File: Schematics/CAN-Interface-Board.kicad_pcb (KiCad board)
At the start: 4 copper layers, 165.1 x 100 mm, 56 parts, among them CN1 Limit Switch Connector 1, CN2 Limit Switch Connector 2, CN3 Encoder Connector, CN5 XY-B3B-XH-A, CN6 MOLEX_26013114, CN7 MOLEX_CAN_IN, CN8 MOLEX_CAN_OUT, J1 USB_C_Receptacle, J2 Conn_01x04_Pin, J4 Conn_01x04_Pin, Q1 INA180A2, U1 SN65HVD230, U2 LD1117S33TR, U3 STM32F405RGTx

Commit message: inital layout started, refining stage
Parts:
- removed CBulk1: 4.7u, Capacitor_SMD:C_0805_2012Metric_Pad1.18x1.45mm_HandSolder
- removed CN5: XY-B3B-XH-A, custom footprints:CONN-TH_3P-P2.50_A2501WV2-3P
- removed CN6: MOLEX_26013114, custom footprints:MOLEX 26013114
- removed CN7: MOLEX_CAN_IN, custom footprints:MOLEX 26013114
- removed CN8: MOLEX_CAN_OUT, custom footprints:MOLEX 26013114
- removed J4: Conn_01x04_Pin, Connector_PinHeader_2.54mm:PinHeader_1x04_P2.54mm_Vertical
- added BootSwitch1: SAMZO G4R0015010, myFootprints:SAMZO G4R0015010, F.Cu at (153.2, 86.0)
- added C18: 100nf, Capacitor_SMD:C_0805_2012Metric_Pad1.18x1.45mm_HandSolder, F.Cu at (144.2, 58.8)
- added C20: 18p, Capacitor_SMD:C_0805_2012Metric_Pad1.18x1.45mm_HandSolder, F.Cu at (146.6, 55.0)
- added C21: 100nf, Capacitor_SMD:C_0805_2012Metric_Pad1.18x1.45mm_HandSolder, F.Cu at (130.1, 72.4)
- added C22: 100nf, Capacitor_SMD:C_0805_2012Metric_Pad1.18x1.45mm_HandSolder, F.Cu at (130.1, 75.4)
- added C23: 100nf, Capacitor_SMD:C_0805_2012Metric_Pad1.18x1.45mm_HandSolder, F.Cu at (130.1, 78.4)
- added C24: 100nf, Capacitor_SMD:C_0805_2012Metric_Pad1.18x1.45mm_HandSolder, F.Cu at (130.0, 64.4)
- added C25: 100nf, Capacitor_SMD:C_0805_2012Metric_Pad1.18x1.45mm_HandSolder, F.Cu at (130.0, 67.4)
- added C26: 1uf, Capacitor_SMD:C_0805_2012Metric_Pad1.18x1.45mm_HandSolder, F.Cu at (145.8, 94.0)
- added C27: 100nf, Capacitor_SMD:C_0805_2012Metric_Pad1.18x1.45mm_HandSolder, F.Cu at (145.8, 101.0)
- added C28: 1uf, Capacitor_SMD:C_0805_2012Metric_Pad1.18x1.45mm_HandSolder, F.Cu at (145.8, 103.2)
- added C29: 47uf, Capacitor_SMD:C_0805_2012Metric_Pad1.18x1.45mm_HandSolder, F.Cu at (145.8, 105.5)
- added C30: 4.7u, Capacitor_SMD:C_0805_2012Metric_Pad1.18x1.45mm_HandSolder, F.Cu at (141.2, 72.8)
- added CAN_IN1: CAN, myFootprints:MOLEX_26013114, F.Cu at (148.1, 44.2)
- added CAN_OUT1: CAN, myFootprints:MOLEX_26013114, F.Cu at (138.7, 44.2)
- added CN4: XY-B3B-XH-A, myFootprints:JST_B3B-XH-A, F.Cu at (156.2, 106.0)
- added D2: D_Schottky, Diode_SMD:D_2114_3652Metric, F.Cu at (120.5, 85.5)
- added D4: SRV05-4.TCT, myFootprints:SOT95P280X145-6N, F.Cu at (120.9, 70.8)
- added J3: Micro_SD_Card, Connector_Card:microSD_HC_Molex_104031-0811, F.Cu at (116.0, 54.5)
- added PowerIn1: 2 pin Molex, myFootprints:MOLEX_26013114, F.Cu at (142.6, 115.6)
- added R10: 10k, Resistor_SMD:R_0805_2012Metric_Pad1.20x1.40mm_HandSolder, F.Cu at (134.8, 68.5)
- added R13: 10k, Resistor_SMD:R_0805_2012Metric_Pad1.20x1.40mm_HandSolder, F.Cu at (112.5, 94.5)
- added R9: 10k, Resistor_SMD:R_0805_2012Metric_Pad1.20x1.40mm_HandSolder, F.Cu at (125.2, 52.4)
- added RSTSwitch1: SAMZO G4R0015010, myFootprints:SAMZO G4R0015010, F.Cu at (153.2, 80.5)
- added U4: MPL3115A2R1, myFootprints:PSON80P300X300X100-8N, F.Cu at (134.8, 74.0)
- added U5: LSM6DS3TR-C, myFootprints:LGA-14-2.5X3MM, F.Cu at (135.0, 65.0)
- added U6: TPS22917DBVR, myFootprints:SOT95P280X145-6N, F.Cu at (145.8, 97.2)
- added Y1: 8mhz, Crystal:Crystal_SMD_3225-4Pin_3.2x2.5mm_HandSoldering, F.Cu at (150.5, 54.8)
- C1, C2: value 100nF -> 100nf
- C10: value 2.2u -> 100nf
- C13, C17: value 100nf -> 1u
- C16, C7: value 1u -> 100nf
- C19: value 100nf -> 18p; footprint Resistor_SMD:R_0805_2012Metric_Pad1.20x1.40mm_HandSolder -> Capacitor_SMD:C_0805_2012Metric_Pad1.18x1.45mm_HandSolder
- C3: value 10uF -> 100nf
- C4: value 100nF -> 1u
- C5: value 100nF -> 4.7u
- C8: value 100nf -> 2.2u
- CN1, CN2: footprint custom footprints:JST B2B-XH-A(LF)(SN) -> myFootprints:JST_B2B-XH-A_LF__SN_
- CN3: value Encoder Connector -> XY-B3B-XH-A; footprint custom footprints:CONN-TH_S05B-PASK-2-LF-SN -> myFootprints:JST_B3B-XH-A
- D1: value SRV05-4.TCT -> D_Schottky; footprint custom footprints:SOT-23-6_L2.9-W1.6-P0.95-LS2.8-BR -> Diode_SMD:D_2114_3652Metric
- J1: value USB_C_Receptacle -> Microsemi_FlashPro-JTAG-10; footprint Connector_USB:USB_C_Receptacle_HRO_TYPE-C-31-M-12 -> myFootprints:CONN_7024610XX_MOL
- J2: value Conn_01x04_Pin -> USB_C_Receptacle; footprint Connector_PinHeader_2.54mm:PinHeader_1x04_P2.54mm_Vertical -> Connector_USB:USB_C_Receptacle_HRO_TYPE-C-31-M-12
- R1: value 120R -> 150r; footprint Resistor_SMD:R_0603_1608Metric -> Resistor_SMD:R_0805_2012Metric_Pad1.20x1.40mm_HandSolder
- R11: value 1k -> 100k
- R12: value .33k -> 10k
- R2: value 10K -> 120r
- R3: value 10K -> 10k
- R4: value 0.015Ohm -> 100k; footprint Resistor_SMD:R_1206_3216Metric -> Resistor_SMD:R_0805_2012Metric_Pad1.20x1.40mm_HandSolder
- R5: value 10k -> 1k
- R6: value 100k -> 5.1k
- R8: value 5.1k -> 33r
- U2: value LD1117S33TR -> LDL1117-3.3; footprint Package_TO_SOT_SMD:SOT-223-3_TabPin2 -> myFootprints:SOT230P700X180-4N
- U3: value STM32F405RGTx -> STM32F405RGT6
- moved CN1 167.3 mm to (113.2, 116.0)
- moved CN2 164.4 mm to (113.2, 100.5)
- moved R5 148.8 mm to (113.5, 82.2), turned to 0 degrees
- moved R12 147.7 mm to (112.8, 110.0), turned to -90 degrees
- moved C6 147.5 mm to (114.5, 90.8), turned to 0 degrees
- moved PowerLED1 145.5 mm to (112.8, 80.0), turned to 0 degrees
- moved J_BUCK_OUT_B1 142.6 mm to (120.3, 91.5), turned to 90 degrees
- moved D3 141.2 mm to (113.2, 87.5), turned to 0 degrees
- moved R6 134.0 mm to (117.4, 75.5), turned to 180 degrees
- moved J_BUCK_OUT_A1 131.3 mm to (133.7, 91.5), turned to 90 degrees
- moved R2 126.2 mm to (154.2, 50.7)
- moved C4 125.9 mm to (135.2, 79.5), turned to 0 degrees
- moved R8 125.3 mm to (125.2, 55.9), turned to 0 degrees
- moved D1 122.9 mm to (127.0, 87.0), turned to 0 degrees
- moved R7 122.1 mm to (118.7, 62.5), turned to 180 degrees
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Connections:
- net /CANL renamed /CAN Transciever/CANL
- net Current_Sensor_Output renamed /Current Sensor/VoltageADC
- C1 pad 1: +3.3V -> +5V
- C1 pad 2: GND -> +5V
- C10 pad 1: Net-(U3-VCAP_2) -> +3.3V
- C13 pad 1: +3.3V -> GND
- C13 pad 2: GND -> +3.3V
- C14 pad 1: +3.3V -> GND
- C14 pad 2: GND -> +3.3VA
- C17 pad 1: +3.3V -> +3.3VA
- C19 pad 1: GND -> /MCU/OSC IN
- C19 pad 2: +5V -> GND
- C3 pad 1: VCC -> +3.3V
- C4 pad 1: +5V -> Net-(D1-K)
- C4 pad 2: Servo_VCC -> GND
- C6 pad 1: /MCU/NRST -> GND
- C6 pad 2: Net-(C6-Pad2) -> +3.3V
- C7 pad 1: GND -> /MCU/NRST
- C7 pad 2: +3.3V -> Net-(C7-Pad2)
- C8 pad 1: GND -> Net-(U3-VCAP_1)
- C8 pad 2: +3.3V -> GND
- C9 pad 1: Net-(U3-VCAP_1) -> Net-(U3-VCAP_2)
- CN1 pad 2: Limit_Switch_A -> /MCU/LimitSwitchCAS
- CN2 pad 2: Limit_Switch_B -> /MCU/LimitSwitchRoll
- CN3 pad 1: +3.3V -> GND
- CN3 pad 2: GND -> /Servo/<NO NET>
- CN3 pad 3: ENCODER_A -> /MCU/PWMServo_Roll
- D1 pad 1: /MCU/D+ -> Net-(D1-K)
- D1 pad 2: GND -> +BATT
- D3 pad 3: +5V -> +3.3V
- D3 pad 4: Net-(D3-DIN) -> /MCU/RGB_DATA
- FB1 pad 2: +3.3V -> +3.3VA
- J_BUCK_IN_A1 pad 1: /VBAT -> GND
- J_BUCK_IN_B1 pad 1: /VBAT -> +BATT
- J_BUCK_IN_B1 pad 2: GND -> +BATT
- J_BUCK_OUT_A1 pad 1: +5V -> GND
- J_BUCK_OUT_B1 pad 2: GND -> +5V
- Q1 pad 4: Servo_VCC -> +5V
- R1 pad 1: /CANH -> +5V
- R1 pad 2: Net-(JP1-A) -> +5V
- R11 pad 1: Net-(PowerLED1-A) -> /MCU/5Venable
- R12 pad 1: Net-(D3-DIN) -> GND
- R12 pad 2: /MCU/RGB_DATA -> /MCU/LimitSwitchCAS
- R2 pad 1: GND -> /CAN Transciever/CANH
- R2 pad 2: Limit_Switch_B -> Net-(JP1-A)
- R3 pad 1: GND -> +3.3V
- R3 pad 2: Limit_Switch_A -> /MCU/NRST
- R4 pad 1: +5V -> GND
- R4 pad 2: Servo_VCC -> /MCU/BOOT0
- R5 pad 1: +3.3V -> Net-(PowerLED1-A)
- R5 pad 2: /MCU/NRST -> +3.3V
- R6 pad 1: GND -> Net-(J2-CC2)
- R6 pad 2: /MCU/BOOT0 -> GND
- R7 pad 1: Net-(J1-CC2) -> Net-(J2-CC1)
- R8 pad 1: Net-(J1-CC1) -> /FlashSD/SDCLK
- R8 pad 2: GND -> Net-(J3-CLK)
- U1 pad 1: CAN_D -> /CAN Transciever/CAN_TX_2
- U1 pad 4: CAN_R -> /CAN Transciever/CAN_RX_2
- U1 pad 7: /CANH -> /CAN Transciever/CANH
- U1 pad 8: CAN_RS -> GND
- U2 pad 1: GND -> Net-(D1-K)
- U2 pad 2: +3.3V -> GND
- U2 pad 3: VCC -> +3.3V
- U3 pad 10: unconnected-(U3-PC2-Pad10) -> /FlashSD/SDMISO
- U3 pad 11: unconnected-(U3-PC3-Pad11) -> /FlashSD/SDMOSI
- U3 pad 13: +3.3V -> +3.3VA
- U3 pad 14: ENCODER_A -> unconnected-(U3-PA0-Pad14)
- U3 pad 15: ENCODER_B -> unconnected-(U3-PA1-Pad15)
- U3 pad 20: unconnected-(U3-PA4-Pad20) -> +3.3V
- U3 pad 21: CAN_RS -> /IMU/IMU_SCK
- U3 pad 22: unconnected-(U3-PA6-Pad22) -> /IMU/IMU_MISO
- U3 pad 23: Servo_Signal -> /IMU/IMU_MOSI
- U3 pad 26: /MCU/pb0 -> /MCU/PWMServo_Roll
- U3 pad 27: /MCU/pb1 -> /MCU/PWMServo_CAS
- U3 pad 28: /MCU/pb2 -> /MCU/5Venable
- U3 pad 29: unconnected-(U3-PB10-Pad29) -> /FlashSD/SDCLK
- U3 pad 33: CAN_R -> /CAN Transciever/CAN_TX_2
- U3 pad 34: CAN_D -> /CAN Transciever/CAN_RX_2
- U3 pad 42: unconnected-(U3-PA9-Pad42) -> /MCU/VBUS
- U3 pad 43: +5V -> unconnected-(U3-PA10-Pad43)
- U3 pad 44: /MCU/D- -> /USB5V
- U3 pad 5: unconnected-(U3-PH0-Pad5) -> /MCU/OSC IN
- U3 pad 53: /MCU/UART_DEBUG_TX -> unconnected-(U3-PC12-Pad53)
- U3 pad 54: /MCU/UART_DEBUG_RX -> unconnected-(U3-PD2-Pad54)
- U3 pad 55: /MCU/pb3 -> /IMU/IMU_DReady
- U3 pad 56: /MCU/pb4 -> /MCU/LimitSwitchCAS
- U3 pad 57: unconnected-(U3-PB5-Pad57) -> /MCU/LimitSwitchRoll
- U3 pad 58: unconnected-(U3-PB6-Pad58) -> /Barometer/BarometerSCL
- U3 pad 59: unconnected-(U3-PB7-Pad59) -> /Barometer/BarometerSDA
- U3 pad 6: unconnected-(U3-PH1-Pad6) -> /MCU/OSC OUT
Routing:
- net GND: track 40.6 -> 0.00 mm
- net /MCU/D+: track 11.1 -> 0.00 mm, vias 2 -> 0
- net /MCU/D-: track 10.7 -> 0.00 mm
- net Net-(J1-CC1): track 7.68 -> 0.00 mm, vias 2 -> 0
- net Net-(J1-CC2): track 7.18 -> 0.00 mm, vias 2 -> 0
- net +5V: track 6.85 -> 0.00 mm
- added copper zone on In2.Cu, net +3.3V
- added copper zone on In1.Cu, net GND
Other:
- board size 165.1 x 100 mm -> 50 x 100 mm
- board text added: "5V ONLY"
- board text added: "Add right angle headers"
- board text added: "Buck In B1"
- board text added: "Buck Out A1"
- board text added: "Buck Out B1"
- board text added: "DESOLDER ALL back jumper"
- board text added: "For new modules:"
- board text added: "Solder 5v front jumper"
- board text removed: "3.3V"
- board text removed: "CAN IN"
- board text removed: "CAN OUT"
- board text removed: "Encoders"
- board text removed: "GND"
- board text removed: "Limit SW 1"
- board text removed: "Limit SW 2"
- board text removed: "SERVO"
- board text removed: "SWCLK"
- board text removed: "SWIO"

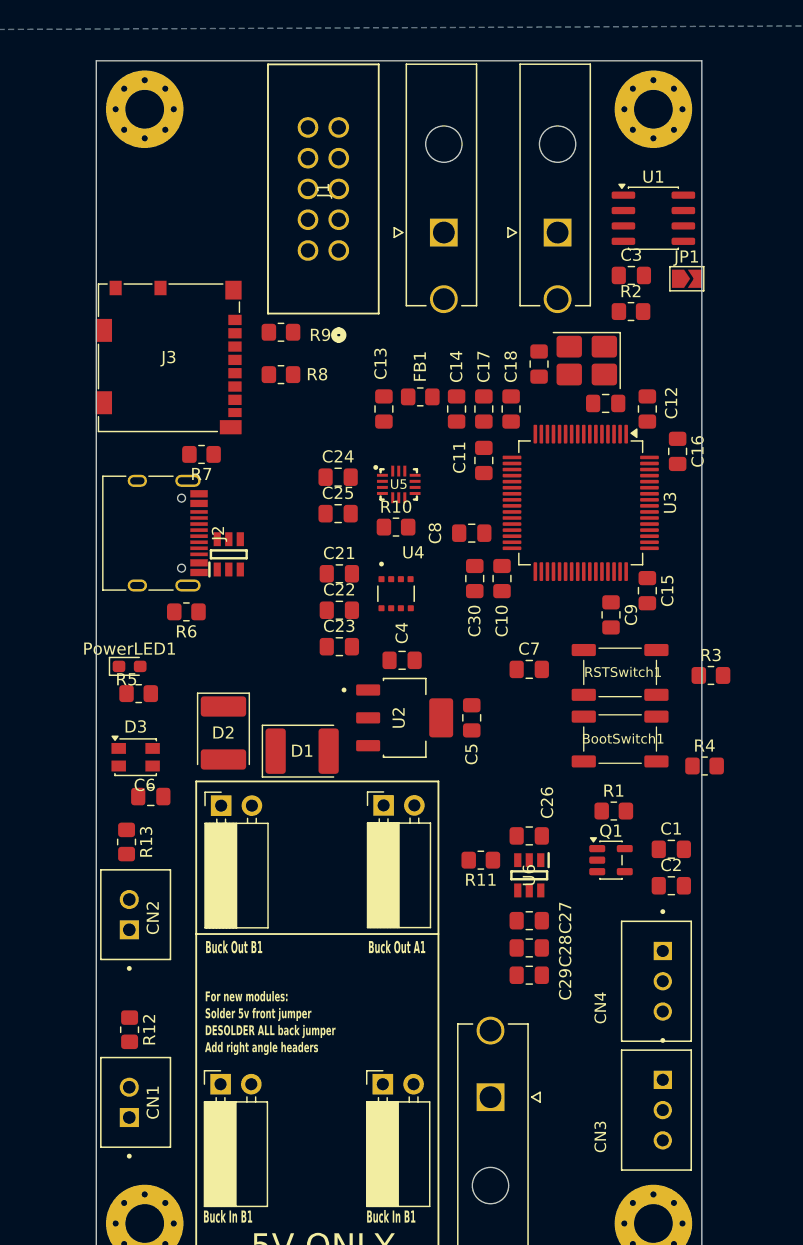
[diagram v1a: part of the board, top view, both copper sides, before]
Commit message: first round of routing complete need to pass DRC first and need to reroute more effiencently
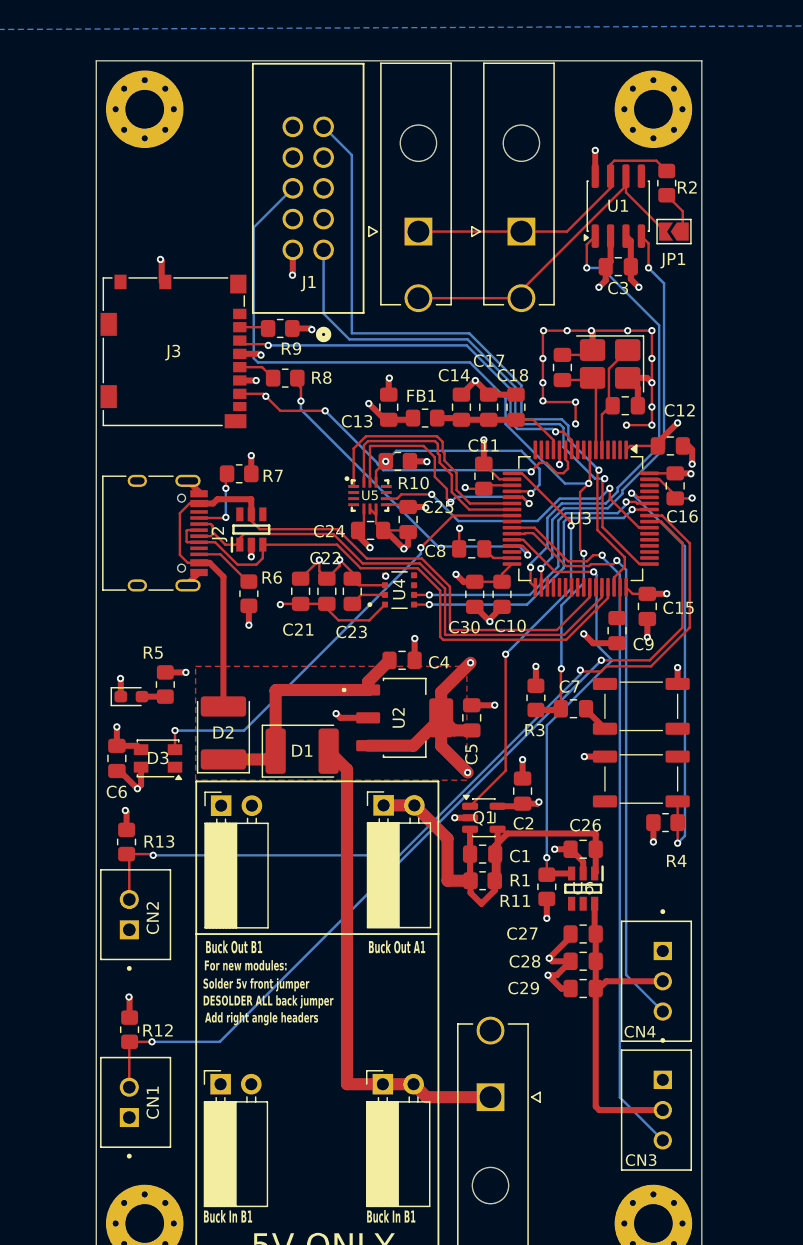
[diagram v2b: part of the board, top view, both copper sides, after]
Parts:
- moved C1 15.6 mm to (141.9, 95.5), turned to 180 degrees
- moved R3 14.6 mm to (146.3, 82.6), turned to -90 degrees
- moved C2 14.6 mm to (145.2, 90.3), turned to 90 degrees
- moved J_BUCK_OUT_A1 13.4 mm to (120.3, 91.5)
- moved J_BUCK_OUT_B1 13.4 mm to (133.7, 91.5)
- moved J_BUCK_IN_A1 13.4 mm to (120.3, 114.5)
- moved J_BUCK_IN_B1 13.4 mm to (133.7, 114.5)
- moved R1 12.3 mm to (141.9, 97.7)
- moved Q1 11.1 mm to (142.0, 92.5)
- moved R2 11.0 mm to (157.1, 40.1), turned to -90 degrees
- moved R11 5.88 mm to (147.2, 98.2), turned to -90 degrees
- moved C25 5.80 mm to (135.8, 67.9), turned to -90 degrees
- moved R4 5.68 mm to (157.0, 92.9)
- moved R10 5.43 mm to (134.9, 63.1), turned to 180 degrees
- moved R6 5.37 mm to (122.6, 74.0), turned to -90 degrees
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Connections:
- D4 pad 1: /MCU/VBUS -> /MCU/D-
- D4 pad 5: +5V -> /USB5V
- J2 pad A6: /MCU/VBUS -> /MCU/D+
- J2 pad A7: /MCU/D+ -> /MCU/D-
- J2 pad B6: /MCU/VBUS -> /MCU/D+
- J2 pad B7: /MCU/D+ -> /MCU/D-
- R10 pad 2: Net-(U5-CS) -> /IMU/IMU_CS
- U3 pad 20: +3.3V -> /IMU/IMU_CS
- U3 pad 42: /MCU/VBUS -> /USB5V
- U3 pad 44: /USB5V -> /MCU/D-
- U5 pad 12: Net-(U5-CS) -> /IMU/IMU_CS
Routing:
- net GND: track 0.00 -> 137.6 mm, vias 0 -> 49
- net +3.3V: track 0.00 -> 90.4 mm, vias 0 -> 23
- net /MCU/LimitSwitchCAS: track 0.00 -> 74.0 mm, vias 0 -> 2
- net /MCU/NRST: track 0.00 -> 73.3 mm, vias 0 -> 3
- net /MCU/LimitSwitchRoll: track 0.00 -> 69.7 mm, vias 0 -> 2
- net /USB5V: track 0.00 -> 62.4 mm
- net /MCU/PWMServo_Roll: track 0.00 -> 59.2 mm, vias 0 -> 1
- net /MCU/SWDIO: track 0.00 -> 56.4 mm, vias 0 -> 1
- net /MCU/PWMServo_CAS: track 0.00 -> 48.8 mm, vias 0 -> 1
- net /MCU/D+: track 0.00 -> 46.7 mm
- net /MCU/SWCLK: track 0.00 -> 45.8 mm, vias 0 -> 1
- net /MCU/D-: track 0.00 -> 44.1 mm
- net +BATT: track 0.00 -> 40.4 mm
- net +5V: track 0.00 -> 40.0 mm
- net /CAN Transciever/CAN_TX_2: track 0.00 -> 39.2 mm, vias 0 -> 2
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- added copper zone on F.Cu, net (none)
